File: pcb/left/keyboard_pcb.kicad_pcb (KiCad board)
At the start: 2 copper layers, 138.8 x 89.9 mm, 101 parts, among them J3 Alt. Battery, J4 Conn_01x01_Socket, K00 KEYSW, K01 KEYSW, K02 KEYSW, K03 KEYSW, K04 KEYSW, K05 KEYSW, K10 KEYSW, K11 KEYSW, K12 KEYSW, K13 KEYSW, K14 KEYSW, K15 KEYSW, K20 KEYSW, K21 KEYSW, K22 KEYSW, K23 KEYSW, K24 KEYSW, K25 KEYSW, K33 KEYSW, K34 KEYSW, K35 KEYSW, U1 Flippable RP2040 ProMicro/nic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

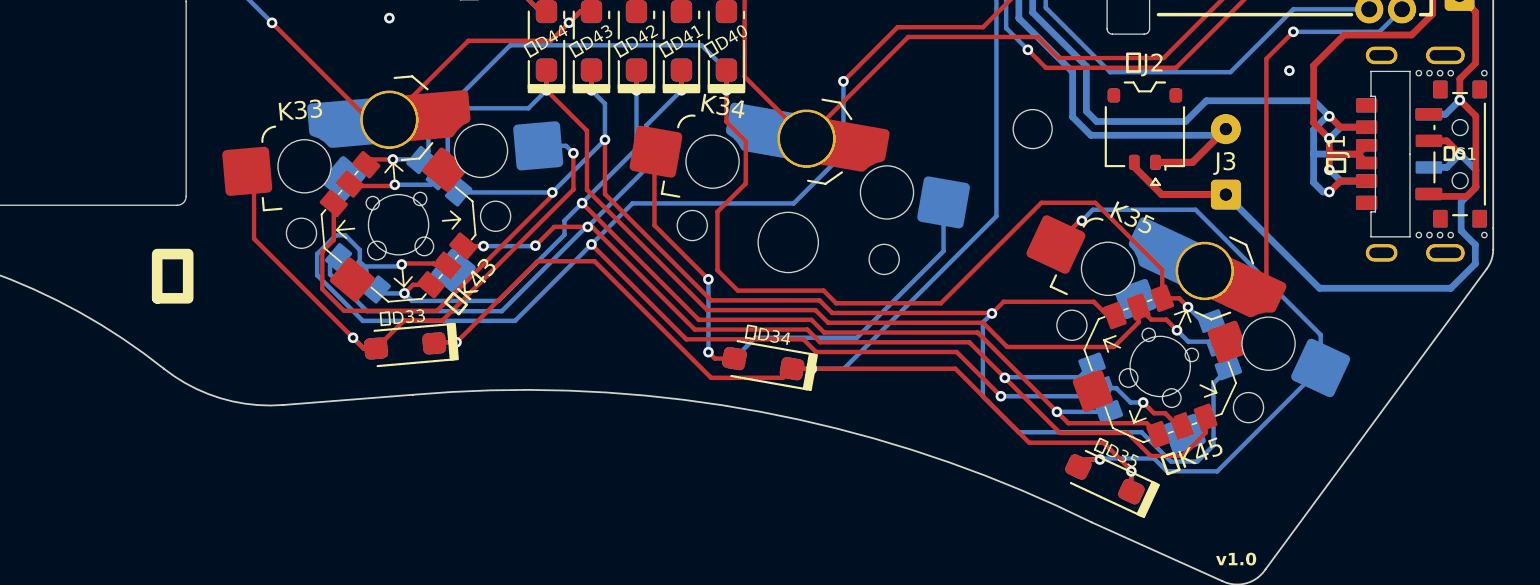
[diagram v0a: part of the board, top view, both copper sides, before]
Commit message: Add alt. battery socket and JLC order number silkscreens
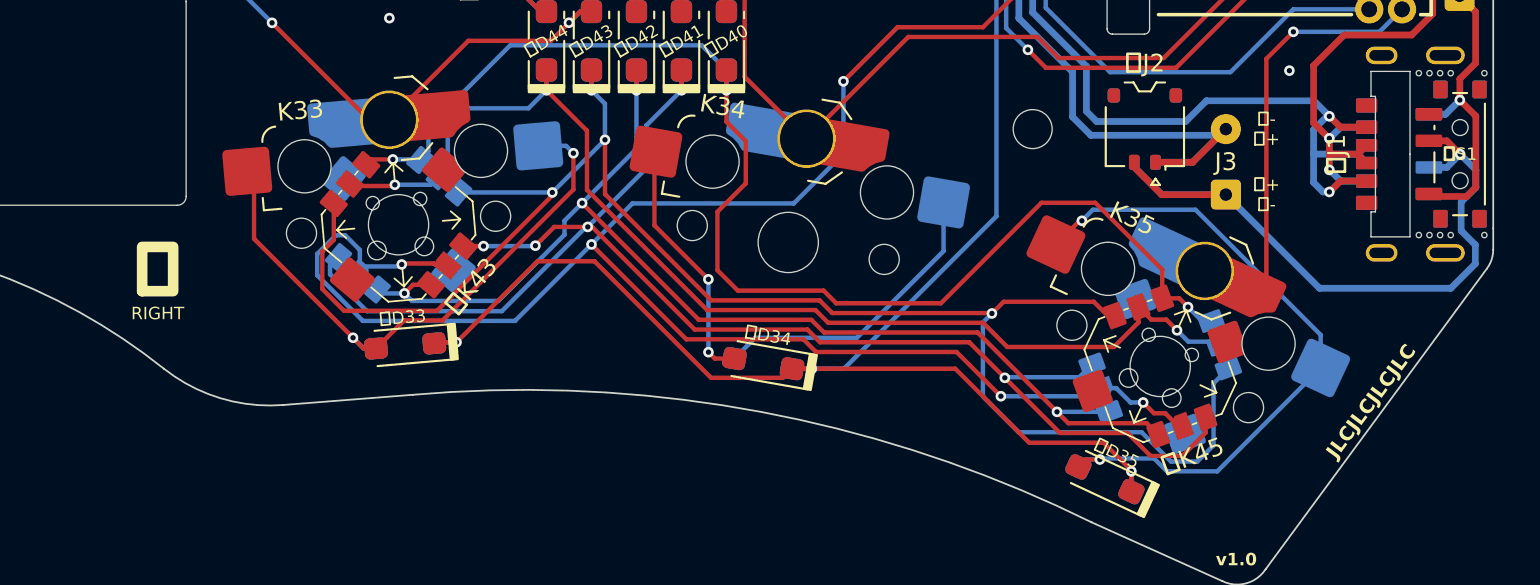
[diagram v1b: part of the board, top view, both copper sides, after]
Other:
- board text added: "JLCJLCJLCJLC"
- board text added: "LEFT"
- board text added: "RIGHT"
- board text added: "左+ 右-"
- board text added: "左- 右+"
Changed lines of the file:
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@@
     (effects (font (size 1 1) (thickness 0.15)) (justify left bottom mirror))
   )
-  (gr_text "左" (at 129.5 116) (layer "B.SilkS")
+  (gr_text "左+\n右-" (at 189.9 111.3) (layer "B.SilkS")
+    (effects (font (size 0.7 0.7) (thickness 0.1)) (justify mirror))
+  )
+  (gr_text "LEFT" (at 127.4 118.0084) (layer "B.SilkS")
+    (effects (font (size 0.7 0.7) (thickness 0.1)) (justify mirror))
+  )
+  (gr_text "左-\n右+" (at 189.9 107.6) (layer "B.SilkS")
+    (effects (font (size 0.7 0.7) (thickness 0.1)) (justify mirror))
+  )
+  (gr_text "左" (at 129.55 115.5936) (layer "B.SilkS")
     (effects (font (size 2.5 2.5) (thickness 0.6) bold) (justify left mirror))
   )
   (gr_text "v1.0" (at 188.3 131.9) (layer "B.SilkS")
     (effects (font (size 0.7 0.7) (thickness 0.12) bold) (justify mirror))
+  )
+  (gr_text "左+\n右-" (at 190 111.3) (layer "F.SilkS")
+    (effects (font (size 0.7 0.7) (thickness 0.1)))
   )
   (gr_text "PROMANTOR" (at 129.3 96.6) (layer "F.SilkS")
@@
     )
   )
-  (gr_text "右" (at 129.5 116) (layer "F.SilkS")
-    (effects (font (size 2.5 2.5) (thickness 0.6) bold) (justify right))
+  (gr_text "RIGHT" (at 127.4 118.0084) (layer "F.SilkS")
+    (effects (font (size 0.7 0.7) (thickness 0.1)))
+  )
+  (gr_text "JLCJLCJLCJLC" (at 195.9 122.963 53.5) (layer "F.SilkS")
+    (effects (font (size 0.8 0.8) (thickness 0.15) bold))
+  )
+  (gr_text "右" (at 127.4 115.5936) (layer "F.SilkS")
+    (effects (font (size 2.5 2.5) (thickness 0.6) bold))
+  )
+  (gr_text "左-\n右+" (at 190 107.6) (layer "F.SilkS")
+    (effects (font (size 0.7 0.7) (thickness 0.1)))
   )
   (gr_text "u/bgkendall" (at 129.3 98.8) (layer "F.SilkS")

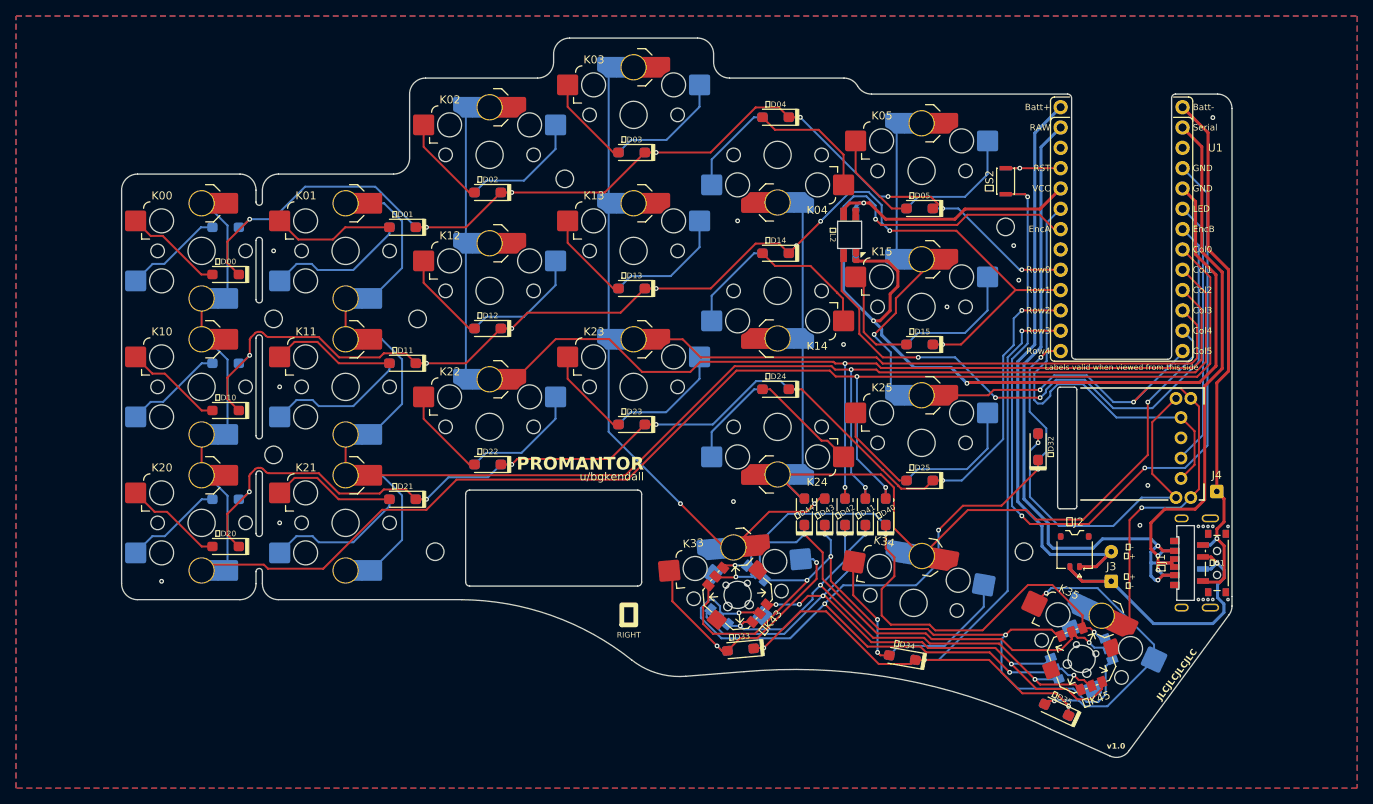
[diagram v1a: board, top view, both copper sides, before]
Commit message: Update track routing
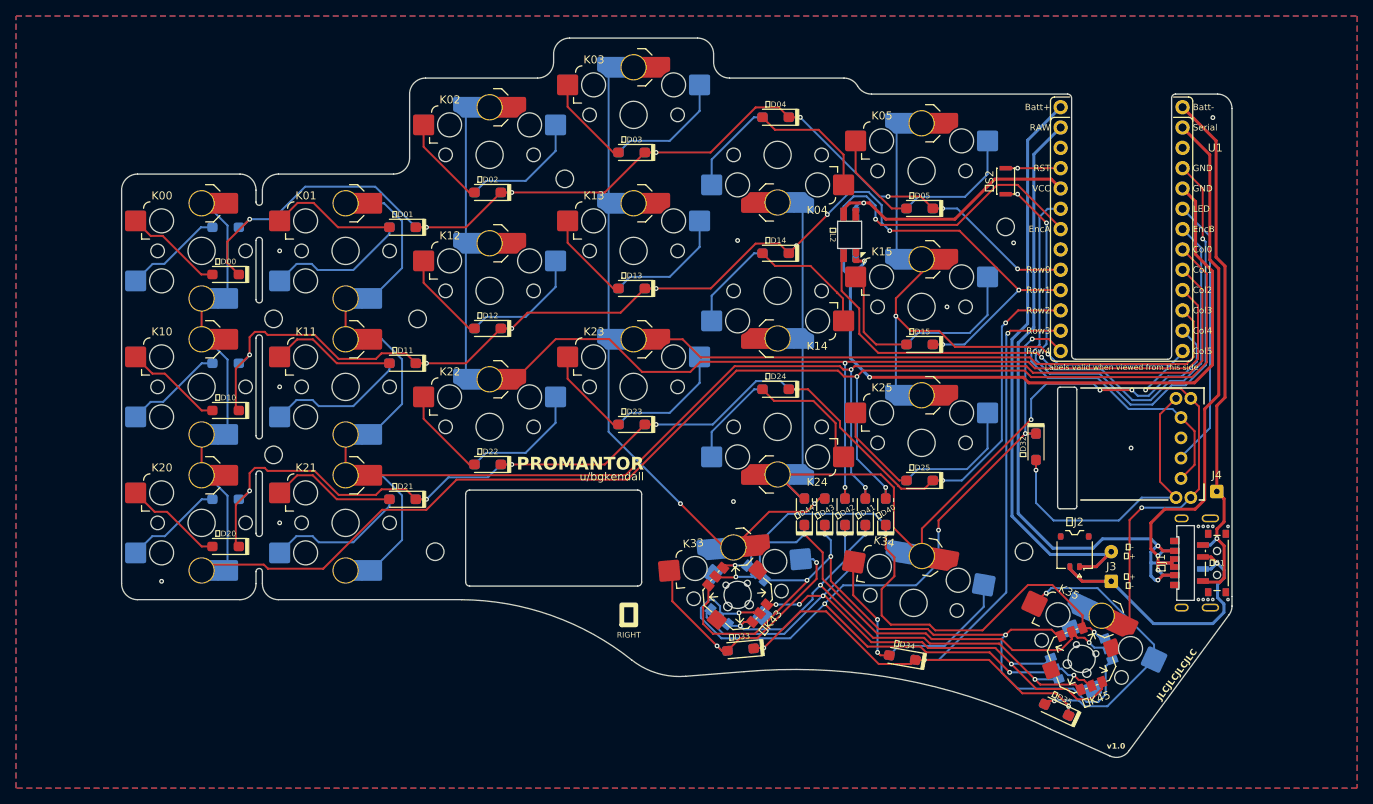
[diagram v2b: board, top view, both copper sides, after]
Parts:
- moved 右D32 0.26 mm to (178.3, 94.5), turned to -90 degrees
- moved 左D32 0.26 mm to (178.3, 94.5), turned to -90 degrees
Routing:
- net reset_gnd: track 110.6 -> 77.2 mm
- net l_3V3/r_gnd: track 94.8 -> 88.1 mm
- net Net-(右D32-A): track 45.6 -> 39.7 mm
- net col5: track 115.7 -> 120.3 mm
- net enc_a: track 55.7 -> 52.2 mm
- net l_led: track 32.4 -> 35.6 mm
- net r_led: track 78.6 -> 76.3 mm, vias 3 -> 1
- net Net-(K24-C): track 13.6 -> 15.5 mm
- net l_gnd/r_3V3: track 32.0 -> 33.0 mm
- net col4: track 123.0 -> 124.0 mm, vias 1 -> 3
- net row3: track 103.3 -> 104.1 mm
- net enc_b: track 33.2 -> 33.9 mm
- net col3: track 157.5 -> 156.8 mm
- net l_data/r_raw: track 83.9 -> 84.5 mm
- net Net-(K01-C): track 15.3 -> 15.9 mm
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
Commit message: Part updates
 * Add LCSC part number property to various parts
 * Update Value for various parts
 * Use SKQGABE010 for reset instead of KXT3
 * Move reset switches to under encoder to accommodate larger switch footprint
 * Re-route reset tracks and some nearby tracks
 * Tweak silkscreens
 * Tweak various routings
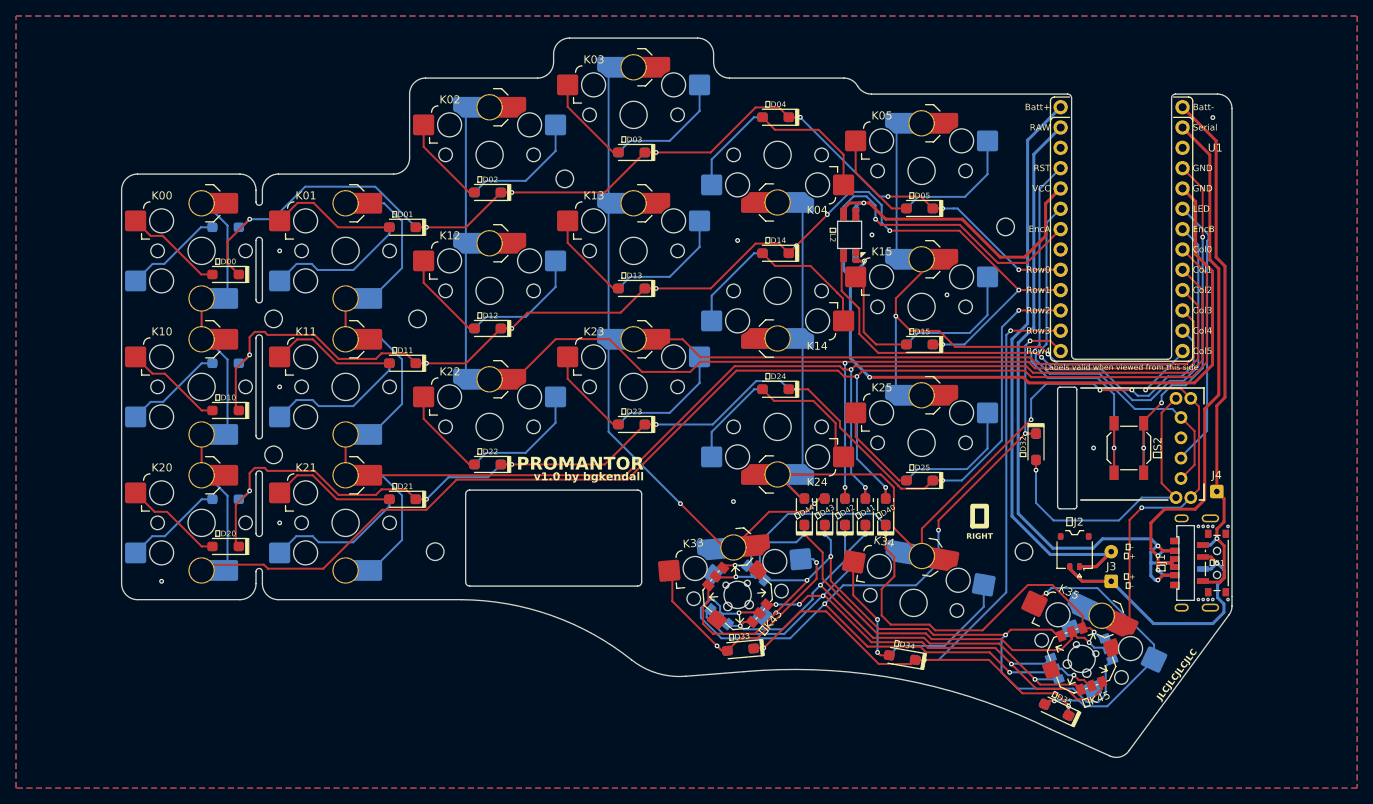
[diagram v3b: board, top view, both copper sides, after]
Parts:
- 右S2, 左S2: footprint Button_Switch_SMD:SW_SPST_CK_KXT3 -> Button_Switch_SMD:SW_SPST_SKQG_WithStem
- moved 右S2 36.7 mm to (189.9, 94.6), turned to -90 degrees
- moved 左S2 36.7 mm to (189.9, 94.6)
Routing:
- net gnd_reset: track 8.38 -> 53.7 mm
- net reset_gnd: track 77.2 -> 49.4 mm
- net l_gnd/r_3V3: track 33.0 -> 38.3 mm
- net enc_a: track 52.2 -> 50.3 mm
- net l_led: track 35.6 -> 34.9 mm
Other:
- board text added: "v1.0 by bgkendall"
- board text removed: "u/bgkendall"
- board text removed: "v1.0"

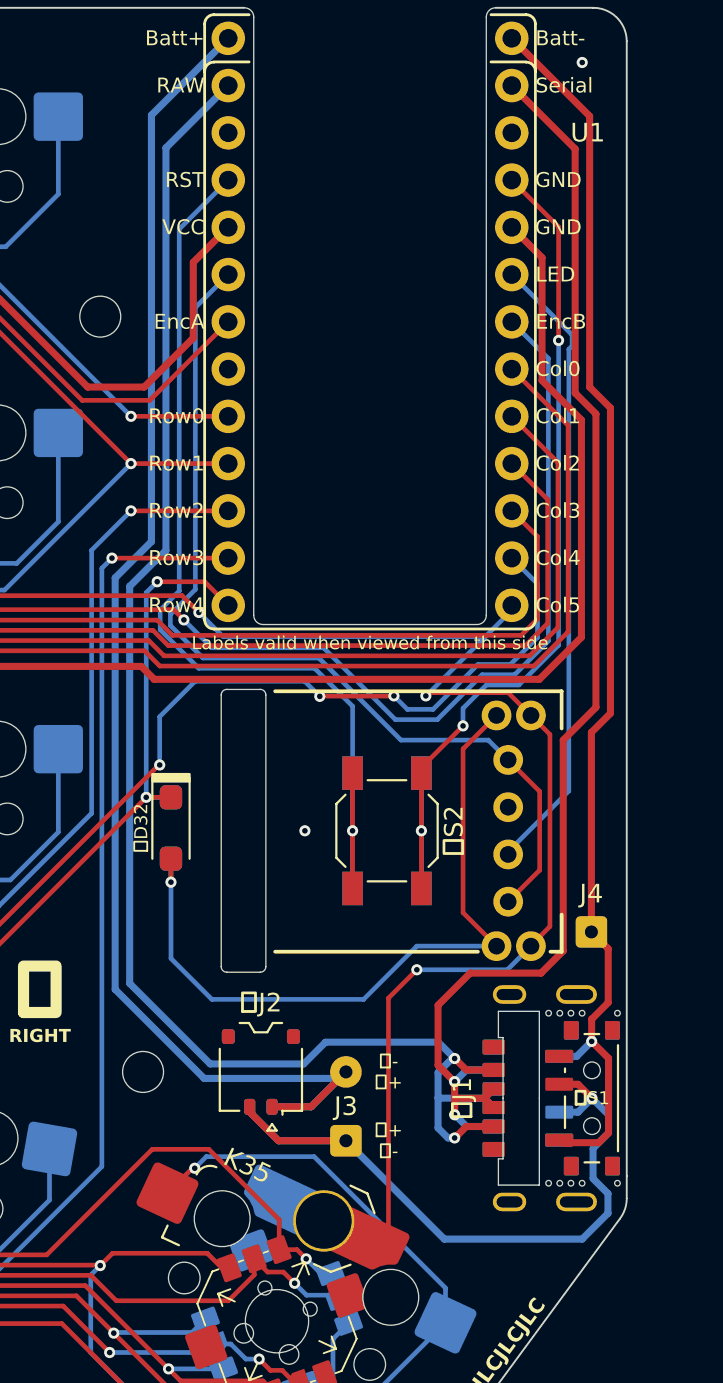
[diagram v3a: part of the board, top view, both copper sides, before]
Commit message: Remove Pico-EZmate connector for battery
The battery terminals can be (carefully) soldered to the board. This is going to be far easier (and cheaper!) than trying to crimp the EZmate terminals (at least without the correct tools).
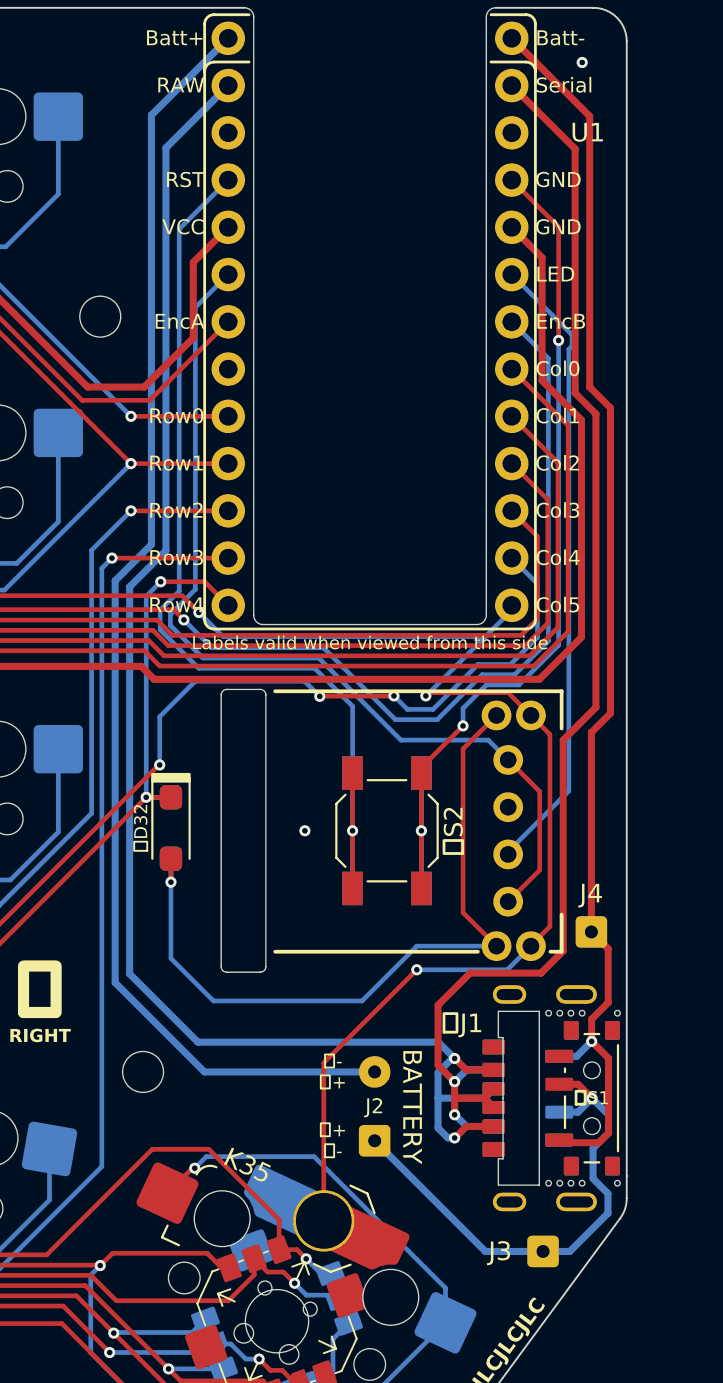
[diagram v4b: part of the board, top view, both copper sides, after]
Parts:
- removed 右J2, 左J2: Conn_01x02_Pin, Connector_Molex:Molex_Pico-EZmate_78171-0002_1x02-1MP_P1.20mm_Vertical
- added J3: Conn_01x01_Socket, Connector_Wire:SolderWire-0.127sqmm_1x01_D0.48mm_OD1mm, F.Cu at (198.3, 117.2)
- E1: value RotaryEncoder_Switch -> EVQWGD001
- J2: renamed from J3; value Alt. Battery -> Battery
- 右K43, 右K45, 左K43, 左K45: value SW_SP5T -> SKRHABE010
- 右S2, 左S2: value SW_Push -> SKQGABE010
- moved J2 1.54 mm to (189.2, 111.3)
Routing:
- net Net-(J2-Pin_1): track 40.1 -> 27.2 mm
- net battery_l-/r+: track 77.7 -> 69.2 mm
- net l_data/r_raw: track 84.5 -> 83.2 mm
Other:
- board text removed: "J3"
- board text removed: "J4"

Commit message: Fix various DRC errors
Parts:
- moved J2 7.01 mm to (182.2, 110.8)
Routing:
- net Net-(J2-Pin_1): track 27.2 -> 34.4 mm
- net battery_l-/r+: track 69.2 -> 62.0 mm
- net Net-(K35-A): track 38.5 -> 37.2 mm
